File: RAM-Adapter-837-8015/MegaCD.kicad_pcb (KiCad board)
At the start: 4 copper layers, 57.9 x 26 mm, 7 parts, among them IC5 MB81C4256Z, IC6 MB81C4256Z, IC7 MB81C4256Z, IC8 MB81C4256Z, U1 HM514270

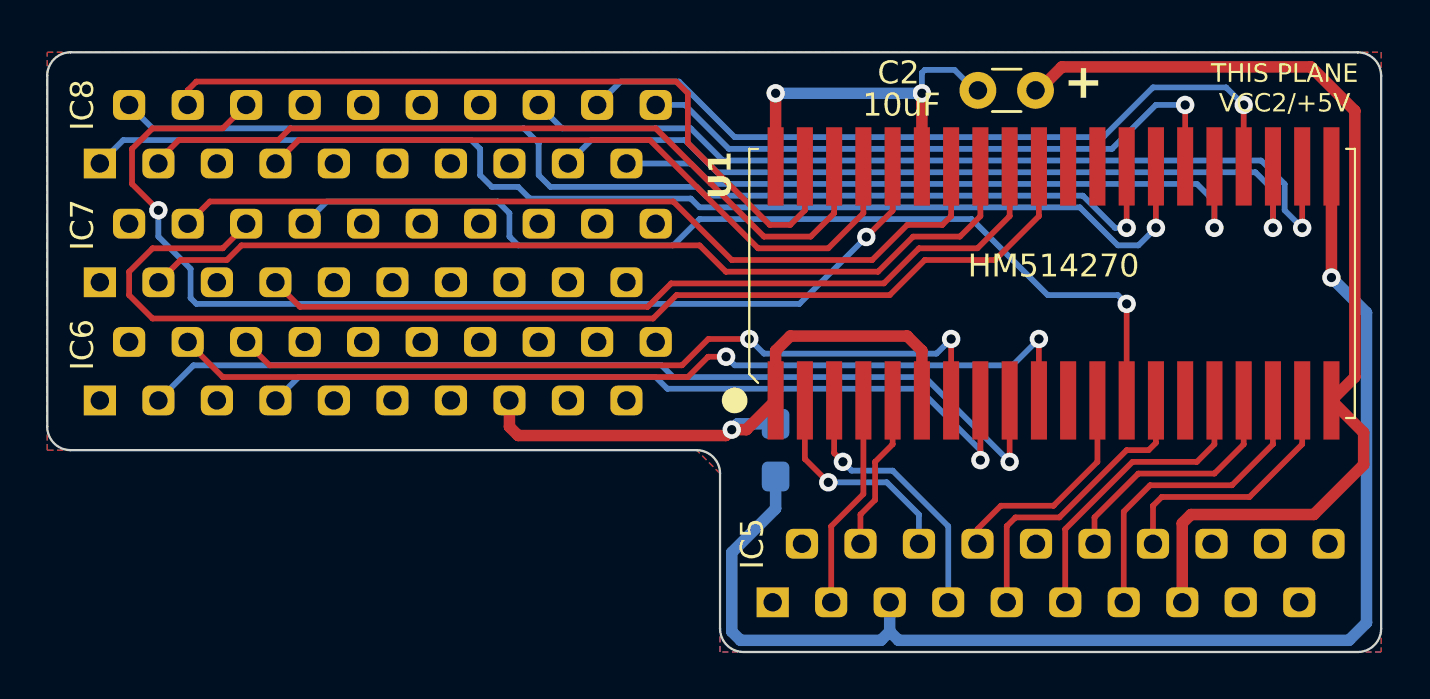
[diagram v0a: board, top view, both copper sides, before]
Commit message: Remove VCC planes from RAM adapter boards.
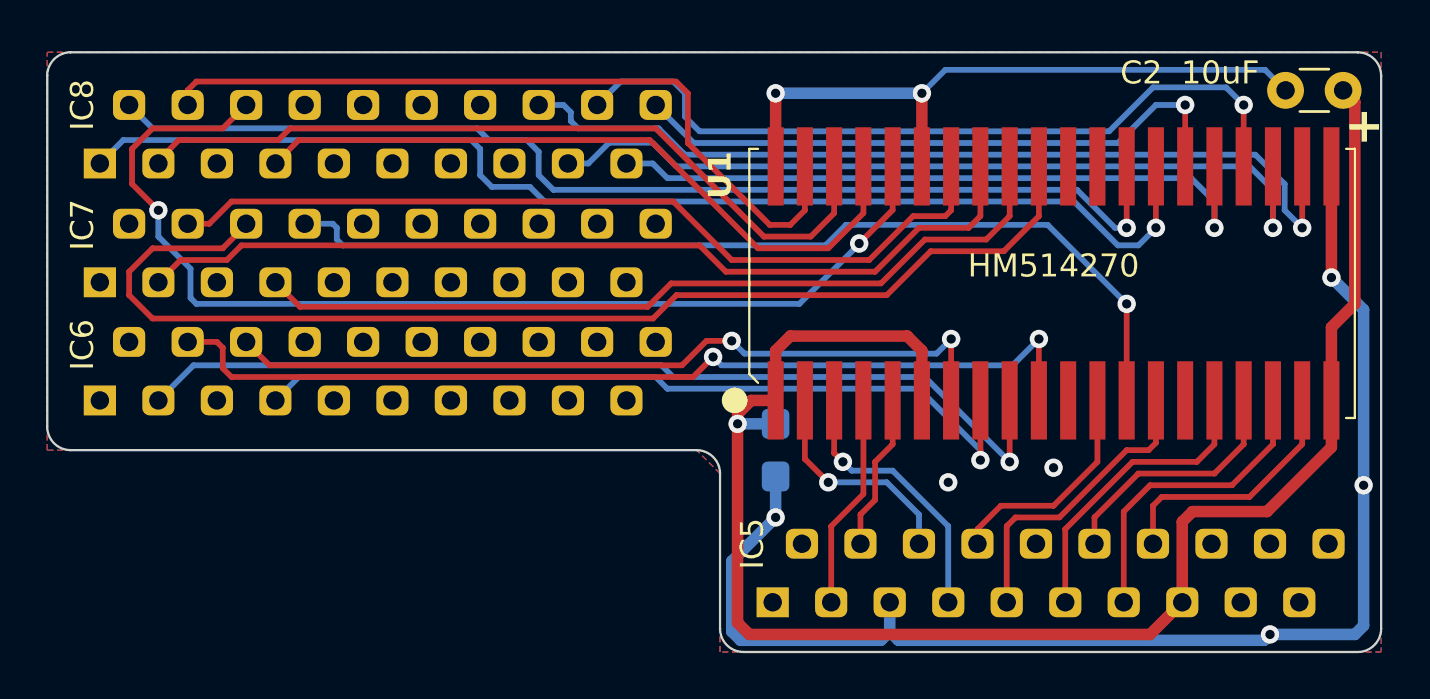
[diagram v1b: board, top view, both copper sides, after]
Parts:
- moved C2 13.4 mm to (173.4, 106.4)
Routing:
- net VCC2: track 80.8 -> 122.1 mm
- net GND: track 84.1 -> 96.8 mm, vias 3 -> 8
- net PA7: track 81.2 -> 86.7 mm
- net PA8: track 76.4 -> 80.4 mm
- net ~{CUWE}: track 48.8 -> 47.5 mm
- net PA6: track 80.6 -> 80.0 mm
- net ~{PRAS}: track 58.6 -> 59.1 mm
- net D7: track 41.2 -> 41.8 mm
- added copper zone on F.Cu, net GND
- removed copper zone on F.Cu, net VCC2
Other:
- board text added: "DO NOT USE THIS LAYER FOR DRC PURPOSES ONLY"
- board text added: "ZIP-TO-SOJ DRAM ADAPTER FOR MEGA-CD 837-8015 REV 1.1 BY COSAM 08/2023"
- board text removed: "THIS PLANE VCC2/+5V"
- board text removed: "ZIP-TO-SOJ DRAM ADAPTER FOR MEGA-CD 837-8015 REV 1.0 BY COSAM 06/2023"
